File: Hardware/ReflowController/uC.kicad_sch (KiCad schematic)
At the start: 0 parts

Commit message: work on uC
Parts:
- added J? (x2): Conn_01x15_Female, symbol Connector:Conn_01x15_Female
- added NT? (x30): NetTie_2, symbol Device:NetTie_2
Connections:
- new net AREF: J?.13 (Pin_13)
- new net NRST_1: J?.3 (Pin_3)
- new net NRST_2: J?.3 (Pin_3)
- new net PA0: J?.12 (Pin_12)
- new net PA1: J?.11 (Pin_11)
- new net PA10: J?.2 (Pin_2)
- new net PA11: J?.13 (Pin_13)
- new net PA12: J?.5 (Pin_5)
- new net PA2: J?.5 (Pin_5)
- new net PA3: J?.10 (Pin_10)
- new net PA4: J?.9 (Pin_9)
- new net PA5: J?.8 (Pin_8)
- new net PA6: J?.7 (Pin_7)
- new net PA7: J?.6 (Pin_6)
- new net PA8: J?.12 (Pin_12)
- new net PA9: J?.1 (Pin_1)
- new net PB0: J?.6 (Pin_6)
- new net PB1: J?.9 (Pin_9)
- new net PB3: J?.15 (Pin_15)
- new net PB4: J?.15 (Pin_15)
- new net PB5: J?.14 (Pin_14)
- new net PB6: J?.8 (Pin_8)
- new net PB7: J?.7 (Pin_7)
- new net PF0: J?.10 (Pin_10)
- new net PF1: J?.11 (Pin_11)
- new net UC_+3.3V: J?.14 (Pin_14)
- new net UC_+5V: J?.4 (Pin_4)
- new net UC_GND: J?.2 (Pin_2), J?.4 (Pin_4)
- new net VIN: J?.1 (Pin_1)

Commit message: defined rough structure with kerem
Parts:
- added NT1: NetTie_2, symbol Device:NetTie_2
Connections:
- net MISO: now also NT?.2
- net MOSI: now also NT?.2
- net PA4: now also NT1.1
- net PA6: now also NT?.1
- net PA7: now also NT?.1
- net SCLK: now also NT1.2
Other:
- moved on the sheet: J?, NT?

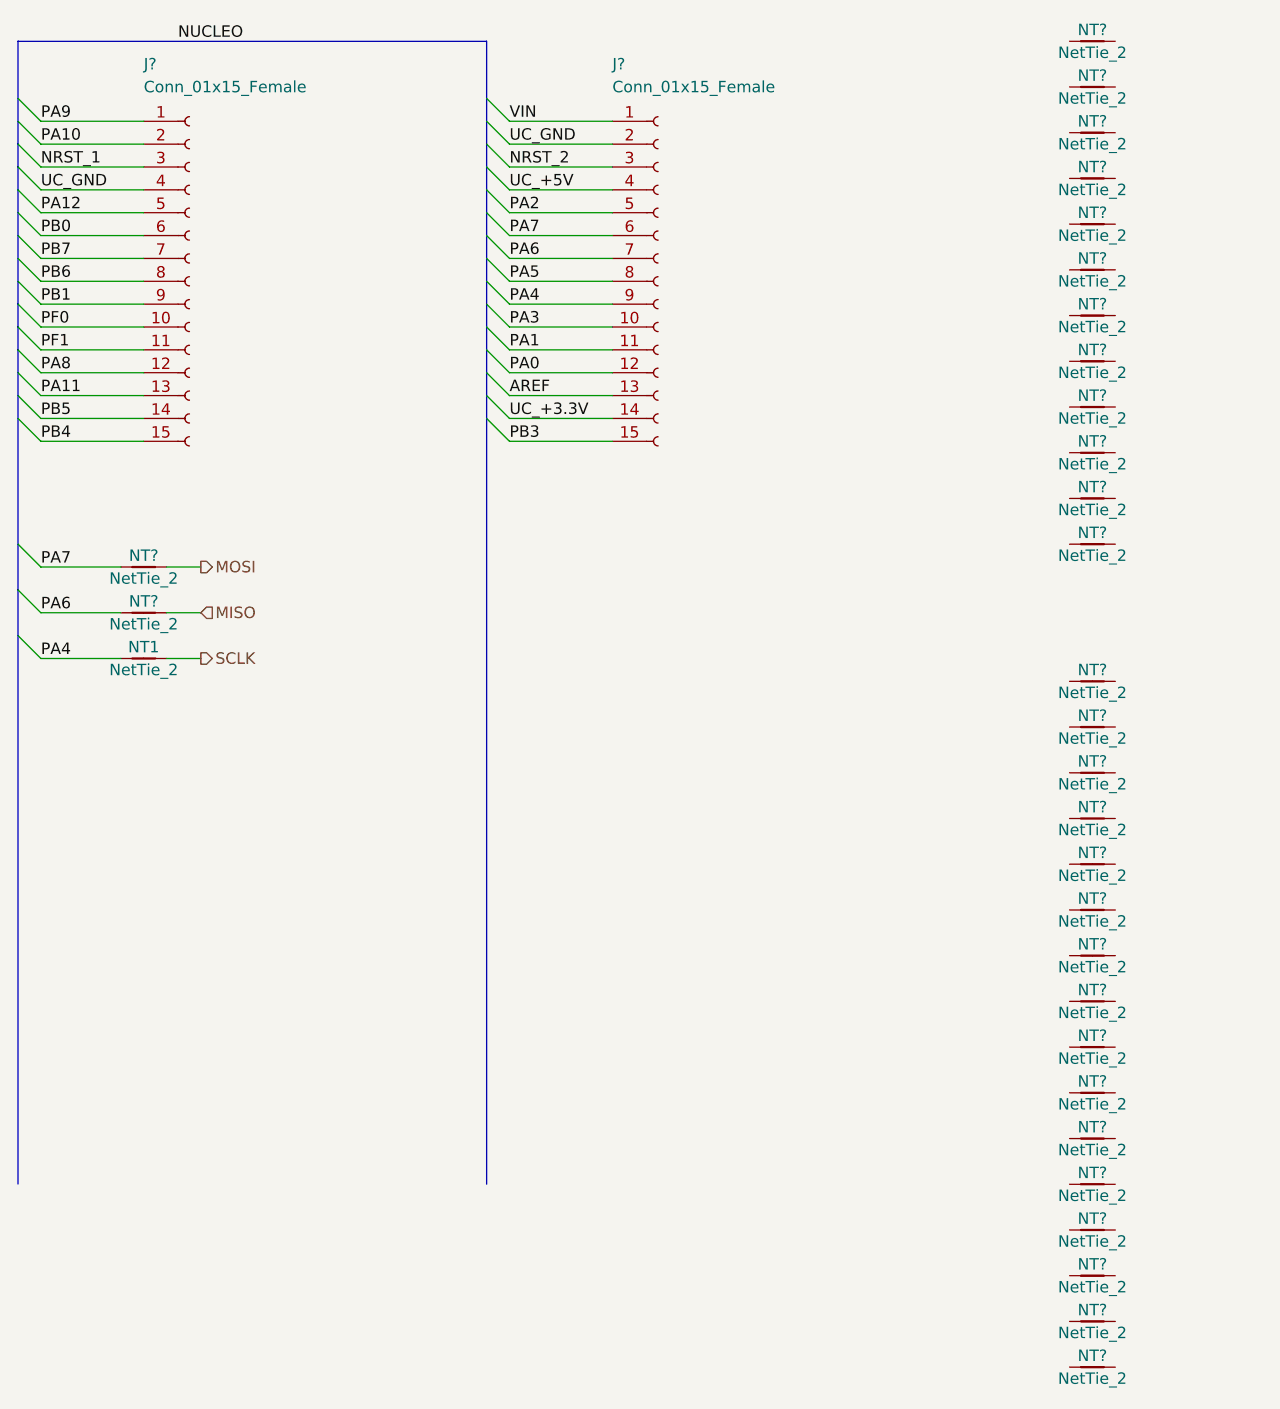
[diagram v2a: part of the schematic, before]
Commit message: Finished the fan controllers calculations, added the wago connectors, added notes
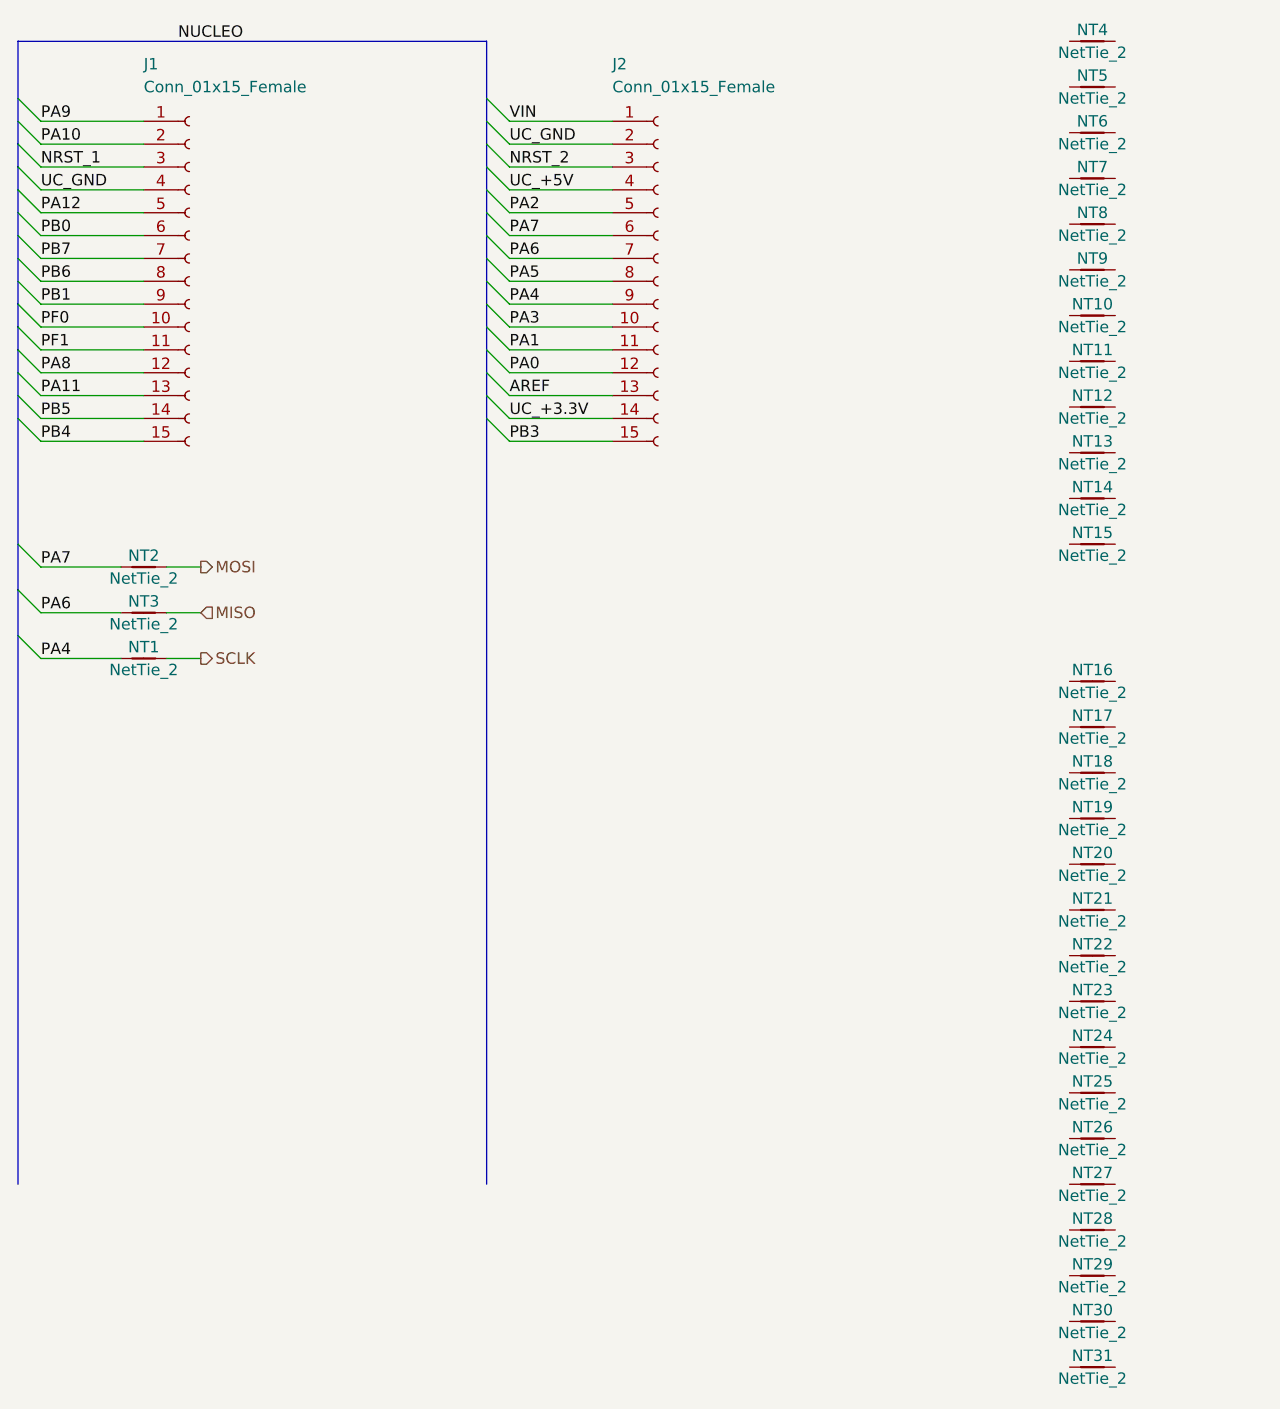
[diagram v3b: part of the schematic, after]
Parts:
- gave numbers to parts that had none: 32
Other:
- title: (none) -> Reflow Oven Control

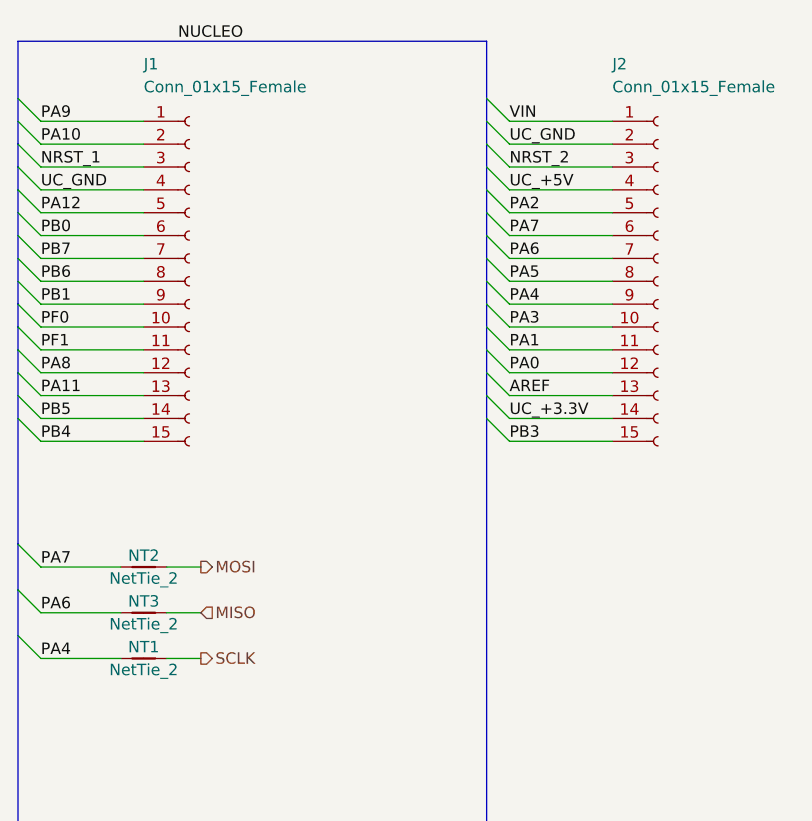
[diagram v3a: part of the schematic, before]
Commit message: finished the io control for the pcb, need to define what is the best way for a remote keypad
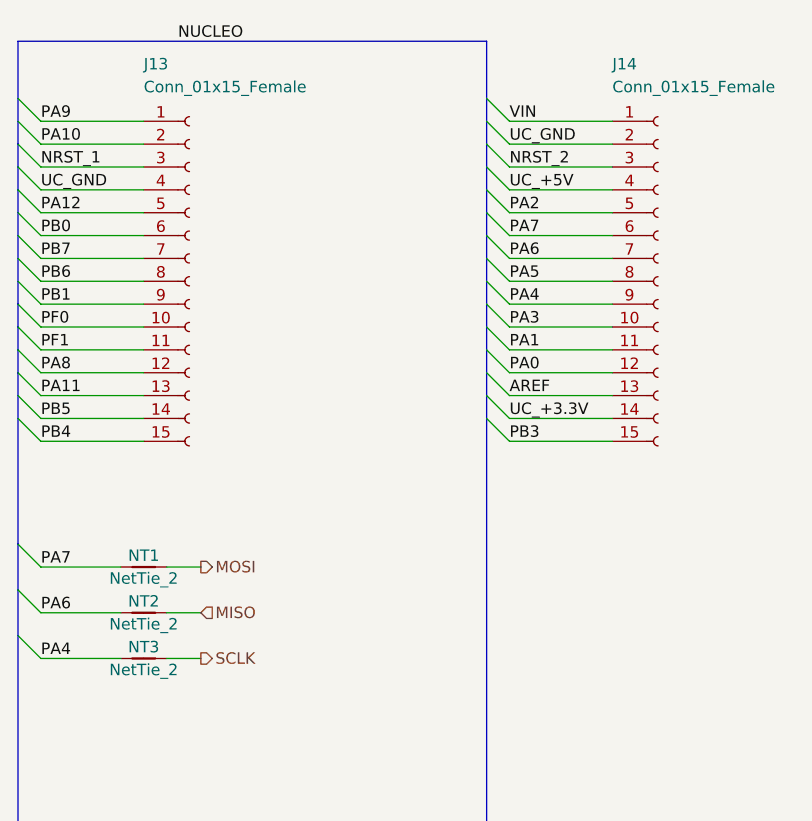
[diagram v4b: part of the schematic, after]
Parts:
- renumbered J1 to J13, J2 to J14, NT2 to NT1, NT3 to NT2, NT1 to NT3
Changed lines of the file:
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@@
   (symbol (lib_id "Device:NetTie_2") (at 39.37 88.9 0) (unit 1)
     (in_bom yes) (on_board yes) (dnp no)
-    (property "Reference" "NT3" (at 39.37 87.63 0)
+    (property "Reference" "NT2" (at 39.37 87.63 0)
       (effects (font (size 1.27 1.27)))
     )
@@
       (project "ReflowController"
         (path "/2394cc2a-b9b0-4c0b-be11-1fc6085b0d5c/7f3c5223-ce8d-4c24-a6f4-4e6402f9b436"
-          (reference "NT3") (unit 1)
+          (reference "NT2") (unit 1)
         )
       )
@@
   (symbol (lib_id "Device:NetTie_2") (at 39.37 83.82 0) (unit 1)
     (in_bom yes) (on_board yes) (dnp no)
-    (property "Reference" "NT2" (at 39.37 82.55 0)
+    (property "Reference" "NT1" (at 39.37 82.55 0)
       (effects (font (size 1.27 1.27)))
     )
@@
       (project "ReflowController"
         (path "/2394cc2a-b9b0-4c0b-be11-1fc6085b0d5c/7f3c5223-ce8d-4c24-a6f4-4e6402f9b436"
-          (reference "NT2") (unit 1)
+          (reference "NT1") (unit 1)
         )
       )
@@
   (symbol (lib_id "Connector:Conn_01x15_Female") (at 44.45 52.07 0) (unit 1)
     (in_bom yes) (on_board yes) (dnp no)
-    (property "Reference" "J1" (at 39.37 27.94 0)
+    (property "Reference" "J13" (at 39.37 27.94 0)
       (effects (font (size 1.27 1.27)) (justify left))
     )
@@
       (project "ReflowController"
         (path "/2394cc2a-b9b0-4c0b-be11-1fc6085b0d5c/7f3c5223-ce8d-4c24-a6f4-4e6402f9b436"
-          (reference "J1") (unit 1)
+          (reference "J13") (unit 1)
         )
       )
@@
   (symbol (lib_id "Connector:Conn_01x15_Female") (at 96.52 52.07 0) (unit 1)
     (in_bom yes) (on_board yes) (dnp no)
-    (property "Reference" "J2" (at 91.44 27.94 0)
+    (property "Reference" "J14" (at 91.44 27.94 0)
       (effects (font (size 1.27 1.27)) (justify left))
     )
@@
       (project "ReflowController"
         (path "/2394cc2a-b9b0-4c0b-be11-1fc6085b0d5c/7f3c5223-ce8d-4c24-a6f4-4e6402f9b436"
-          (reference "J2") (unit 1)
+          (reference "J14") (unit 1)
         )
       )
@@
   (symbol (lib_id "Device:NetTie_2") (at 39.37 93.98 0) (unit 1)
     (in_bom yes) (on_board yes) (dnp no)
-    (property "Reference" "NT1" (at 39.37 92.71 0)
+    (property "Reference" "NT3" (at 39.37 92.71 0)
       (effects (font (size 1.27 1.27)))
     )
@@
       (project "ReflowController"
         (path "/2394cc2a-b9b0-4c0b-be11-1fc6085b0d5c/7f3c5223-ce8d-4c24-a6f4-4e6402f9b436"
-          (reference "NT1") (unit 1)
-        )
-      )
+          (reference "NT3") (unit 1)
+        )
+      )
